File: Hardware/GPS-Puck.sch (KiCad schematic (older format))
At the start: 43 parts, among them J1 Conn-9, Q1 BSS138, Q2 BSS138, U1 Venus838LPx-L, U2 SKY65047-360LF, U3 NCP1521, U4 74HC2G86

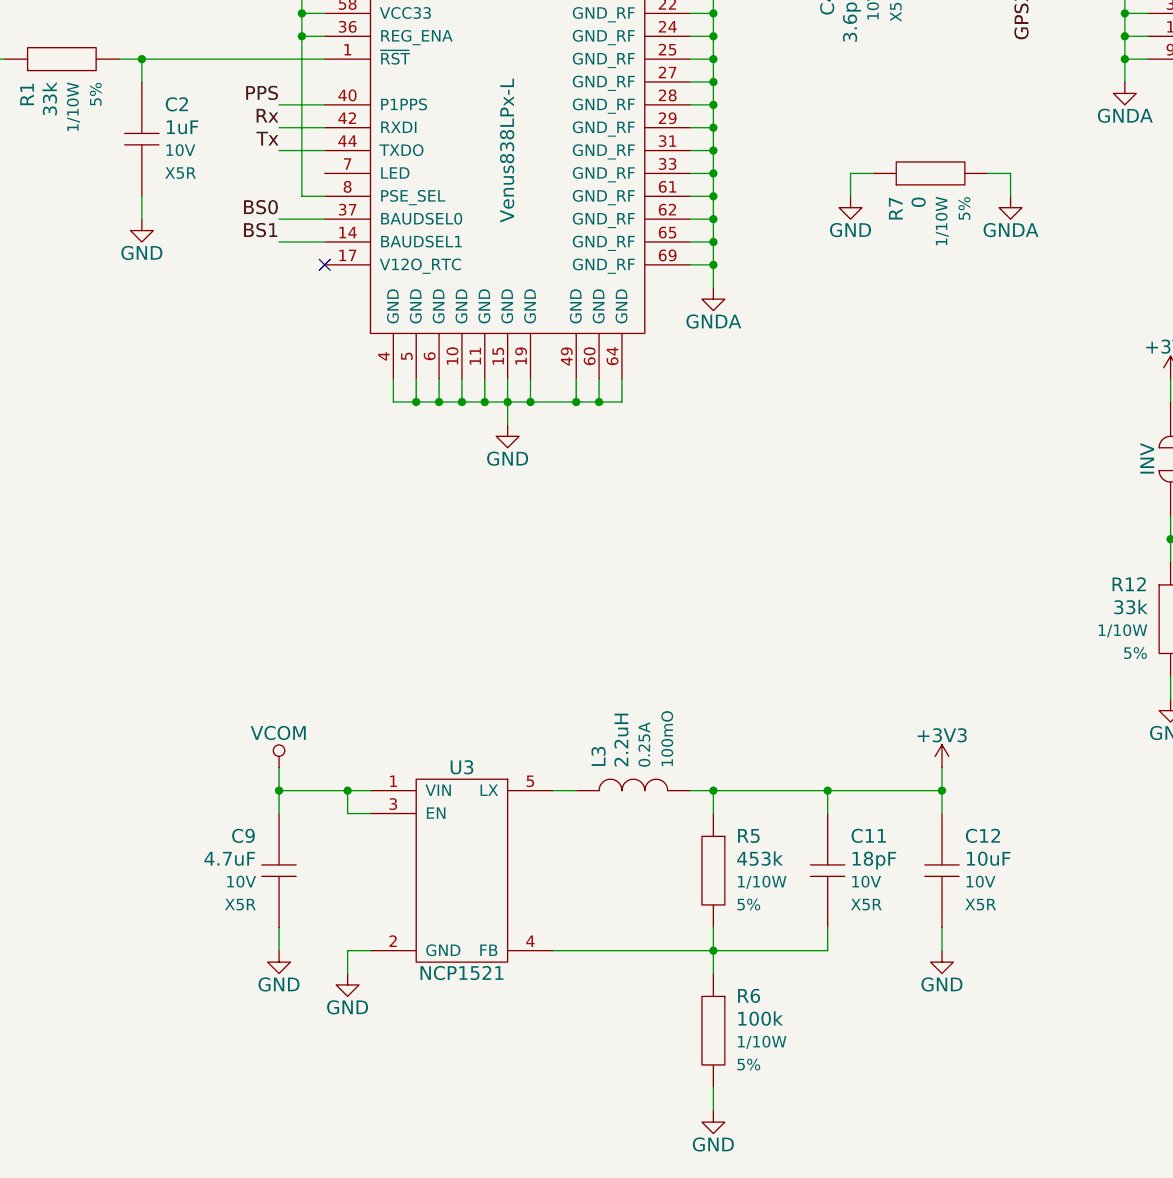
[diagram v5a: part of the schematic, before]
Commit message: Majority layout and routing
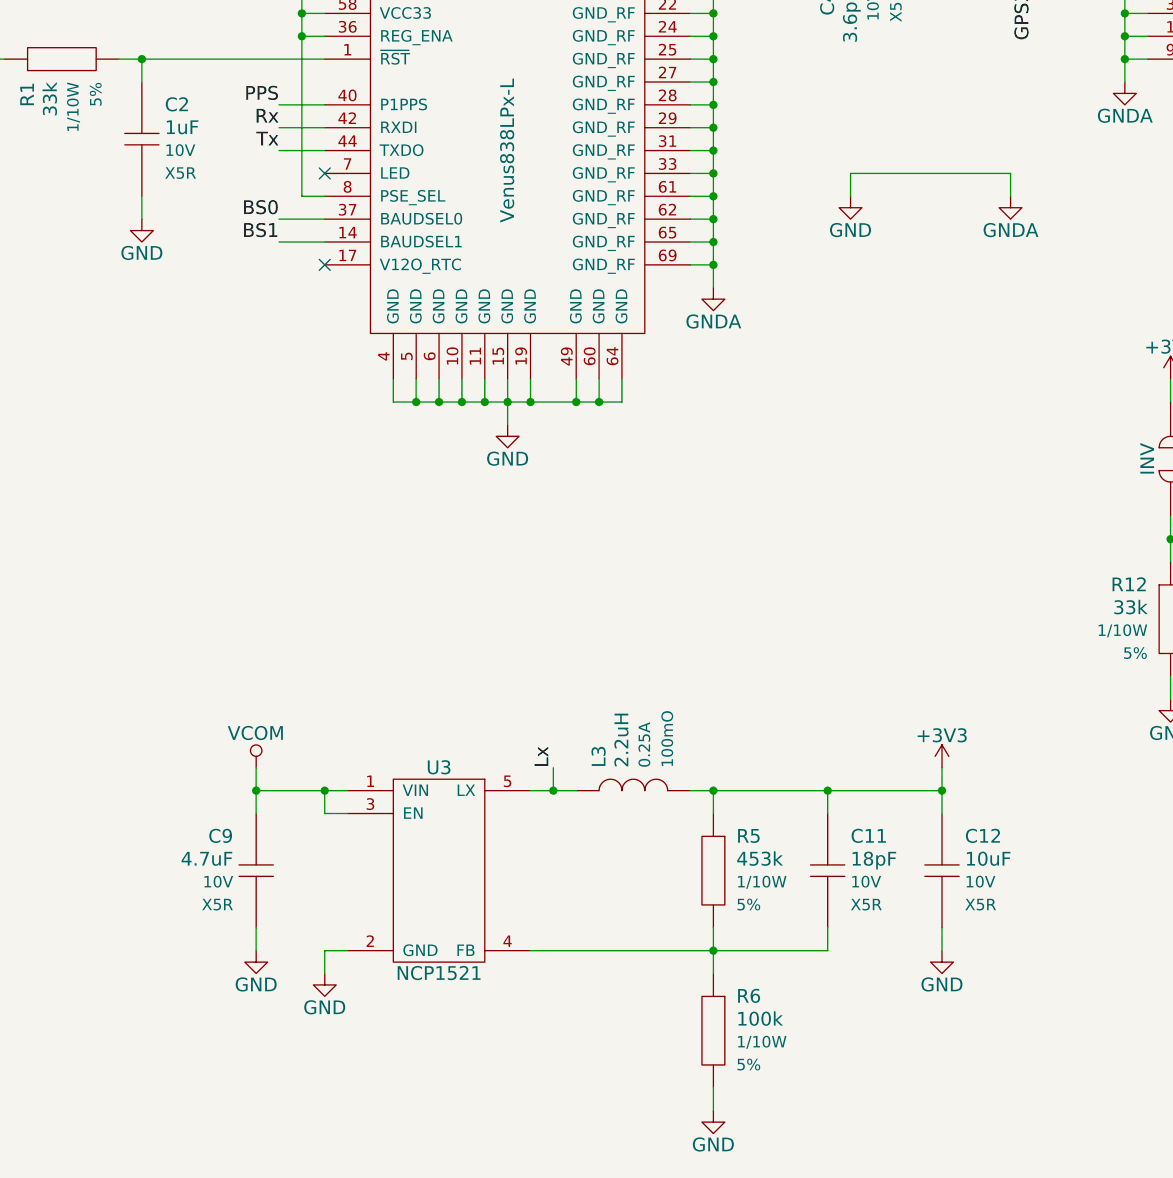
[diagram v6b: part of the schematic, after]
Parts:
- removed R7: 0, Resistors:RESC1608N, symbol Resistor
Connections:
- net GNDA is gone; now on net GND: C3.2, C5.2, C6.2, C7.2, R3.2, U1.21 (GND_RF), U1.22 (GND_RF), U1.24 (GND_RF), U1.25 (GND_RF), U1.27 (GND_RF), U1.28 (GND_RF), U1.29 (GND_RF), U1.31 (GND_RF), U1.33 (GND_RF), U1.61 (GND_RF), U1.62 (GND_RF), U1.65 (GND_RF), U1.69 (GND_RF), U2.1 (GND), U2.3 (GND), U2.4 (GND), U2.9 (PAD)
- net Lx: now reaches L3.1, U3.5 (LX)
- no-connect marks 1 -> 2
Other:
- moved on the sheet: C9, U3
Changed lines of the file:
@@
 L NCP1521 U3
 U 1 1 54A62EE9
-P 3200 6050
-F 0 "U3" H 3200 6500 60  0000 C CNN
-F 1 "NCP1521" H 3200 5600 60  0000 C CNN
-F 2 "SOT:SOT95P275-5L40N" H 3200 6050 60  0001 C CNN
-F 3 "" H 3200 6050 60  0000 C CNN
-	1    3200 6050
+P 3100 6050
+F 0 "U3" H 3100 6500 60  0000 C CNN
+F 1 "NCP1521" H 3100 5600 60  0000 C CNN
+F 2 "SOT:SOT95P275-5L40N" H 3100 6050 60  0001 C CNN
+F 3 "" H 3100 6050 60  0000 C CNN
+	1    3100 6050
 	1    0    0    -1
 $EndComp
@@
 L Capacitor C9
 U 1 1 54A637C4
-P 2400 6050
-F 0 "C9" V 2250 6150 60  0000 L CNN
-F 1 "4.7uF" V 2350 6150 60  0000 L CNN
-F 2 "Capacitors:CAPC1608N" H 2300 6050 60  0001 C CNN
-F 3 "" H 2400 6150 60  0001 C CNN
-F 4 "Value" H 2400 6050 60  0001 C CNN "Manufacturer"
-F 5 "Value" H 2400 6050 60  0001 C CNN "Manufacturer Part #"
-F 6 "Value" H 2400 6050 60  0001 C CNN "Vendor"
-F 7 "Value" H 2400 6050 60  0001 C CNN "Vendor Part #"
-F 8 "10V" V 2450 6150 50  0000 L CNN "Voltage"
-F 9 "X5R" V 2550 6150 50  0000 L CNN "Dielectric"
-	1    2400 6050
+P 2300 6050
+F 0 "C9" V 2150 6150 60  0000 L CNN
+F 1 "4.7uF" V 2250 6150 60  0000 L CNN
+F 2 "Capacitors:CAPC1608N" H 2200 6050 60  0001 C CNN
+F 3 "" H 2300 6150 60  0001 C CNN
+F 4 "Value" H 2300 6050 60  0001 C CNN "Manufacturer"
+F 5 "Value" H 2300 6050 60  0001 C CNN "Manufacturer Part #"
+F 6 "Value" H 2300 6050 60  0001 C CNN "Vendor"
+F 7 "Value" H 2300 6050 60  0001 C CNN "Vendor Part #"
+F 8 "10V" V 2350 6150 50  0000 L CNN "Voltage"
+F 9 "X5R" V 2450 6150 50  0000 L CNN "Dielectric"
+	1    2300 6050
 	0    -1   1    0
 $EndComp
@@
 L GND #PWR016
 U 1 1 54A63837
-P 2700 6500
-F 0 "#PWR016" H 2700 6250 60  0001 C CNN
-F 1 "GND" H 2700 6350 60  0000 C CNN
-F 2 "" H 2700 6500 60  0000 C CNN
-F 3 "" H 2700 6500 60  0000 C CNN
-	1    2700 6500
+P 2600 6500
+F 0 "#PWR016" H 2600 6250 60  0001 C CNN
+F 1 "GND" H 2600 6350 60  0000 C CNN
+F 2 "" H 2600 6500 60  0000 C CNN
+F 3 "" H 2600 6500 60  0000 C CNN
+	1    2600 6500
 	1    0    0    -1
 $EndComp
@@
 L VCOM #PWR017
 U 1 1 54A6384B
-P 2400 5600
-F 0 "#PWR017" H 2400 5450 60  0001 C CNN
-F 1 "VCOM" H 2400 5750 60  0000 C CNN
-F 2 "" H 2400 5600 60  0000 C CNN
-F 3 "" H 2400 5600 60  0000 C CNN
-	1    2400 5600
+P 2300 5600
+F 0 "#PWR017" H 2300 5450 60  0001 C CNN
+F 1 "VCOM" H 2300 5750 60  0000 C CNN
+F 2 "" H 2300 5600 60  0000 C CNN
+F 3 "" H 2300 5600 60  0000 C CNN
+	1    2300 5600
 	1    0    0    -1
 $EndComp
@@
 L GND #PWR018
 U 1 1 54A63AE3
-P 2400 6400
-F 0 "#PWR018" H 2400 6150 60  0001 C CNN
-F 1 "GND" H 2400 6250 60  0000 C CNN
-F 2 "" H 2400 6400 60  0000 C CNN
-F 3 "" H 2400 6400 60  0000 C CNN
-	1    2400 6400
+P 2300 6400
+F 0 "#PWR018" H 2300 6150 60  0001 C CNN
+F 1 "GND" H 2300 6250 60  0000 C CNN
+F 2 "" H 2300 6400 60  0000 C CNN
+F 3 "" H 2300 6400 60  0000 C CNN
+	1    2300 6400
 	1    0    0    -1
 $EndComp
@@
 $EndComp
 $Comp
-L Resistor R7
-U 1 1 54A68195
-P 5250 3000
-F 0 "R7" V 5100 3100 60  0000 L CNN
-F 1 "0" V 5200 3100 60  0000 L CNN
-F 2 "Resistors:RESC1608N" H 5150 3000 60  0001 C CNN
-F 3 "" H 5250 3100 60  0001 C CNN
-F 4 "Value" H 5250 3000 60  0001 C CNN "Manufacturer"
-F 5 "Value" H 5250 3000 60  0001 C CNN "Manufacturer Part #"
-F 6 "Value" H 5250 3000 60  0001 C CNN "Vendor"
-F 7 "Value" H 5250 3000 60  0001 C CNN "Vendor Part #"
-F 8 "1/10W" V 5300 3100 50  0000 L CNN "Power"
-F 9 "5%" V 5400 3100 50  0000 L CNN "Tolerance"
-	1    5250 3000
-	1    0    0    1
-$EndComp
-$Comp
 L GND #PWR023
 U 1 1 54A6822A
@@
 	4300 7000 4300 7100
 Wire Wire Line
-	3600 6400 4800 6400
+	3500 6400 4800 6400
 Wire Wire Line
 	4800 6400 4800 6300
@@
 Connection ~ 4300 5700
 Wire Wire Line
-	3700 5700 3600 5700
-Wire Wire Line
-	2400 5600 2400 5800
-Wire Wire Line
-	2400 5700 2800 5700
-Connection ~ 2400 5700
-Wire Wire Line
-	2800 5800 2700 5800
-Wire Wire Line
-	2700 5800 2700 5700
-Connection ~ 2700 5700
-Wire Wire Line
-	2800 6400 2700 6400
-Wire Wire Line
-	2700 6400 2700 6500
-Wire Wire Line
-	2400 6400 2400 6300
+	3700 5700 3500 5700
+Wire Wire Line
+	2300 5600 2300 5800
+Wire Wire Line
+	2300 5700 2700 5700
+Connection ~ 2300 5700
+Wire Wire Line
+	2700 5800 2600 5800
+Wire Wire Line
+	2600 5800 2600 5700
+Connection ~ 2600 5700
+Wire Wire Line
+	2700 6400 2600 6400
+Wire Wire Line
+	2600 6400 2600 6500
+Wire Wire Line
+	2300 6400 2300 6300
 Wire Wire Line
 	2500 2100 2600 2100
@@
 	3200 1600 3200 1700
 Wire Wire Line
-	5600 3100 5600 3000
-Wire Wire Line
-	5600 3000 5500 3000
-Wire Wire Line
-	5000 3000 4900 3000
+	5600 3000 5600 3100
+Wire Wire Line
+	4900 3000 5600 3000
 Wire Wire Line
 	4900 3000 4900 3100
@@
 Wire Wire Line
 	6300 3900 6300 4000
+Text Label 3600 5600 1    60   ~ 0
+Lx
+Wire Wire Line
+	3600 5600 3600 5700
+Connection ~ 3600 5700
+NoConn ~ 2600 3000
 $EndSCHEMATC
